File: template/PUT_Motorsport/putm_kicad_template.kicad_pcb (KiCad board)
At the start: 2 copper layers, 60 x 40 mm, 4 parts

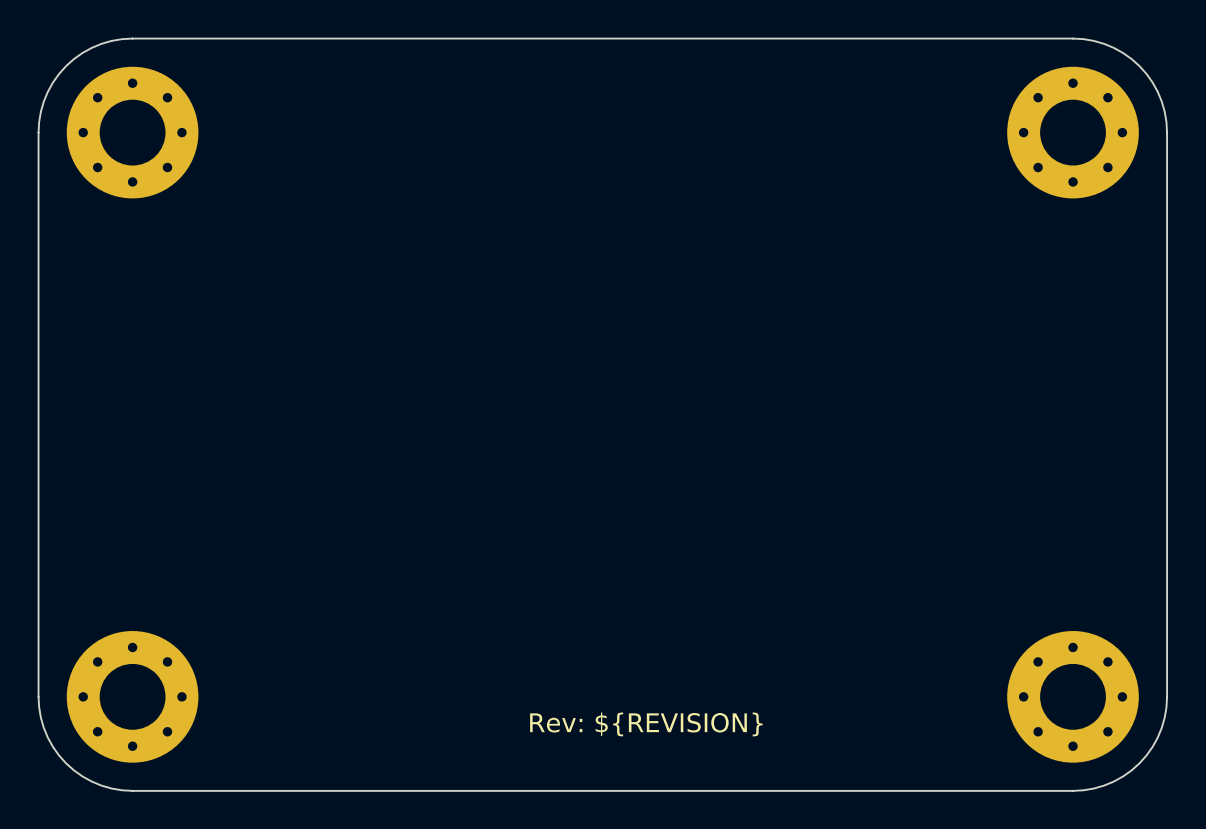
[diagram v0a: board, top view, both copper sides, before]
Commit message: Change mounting holes to M3
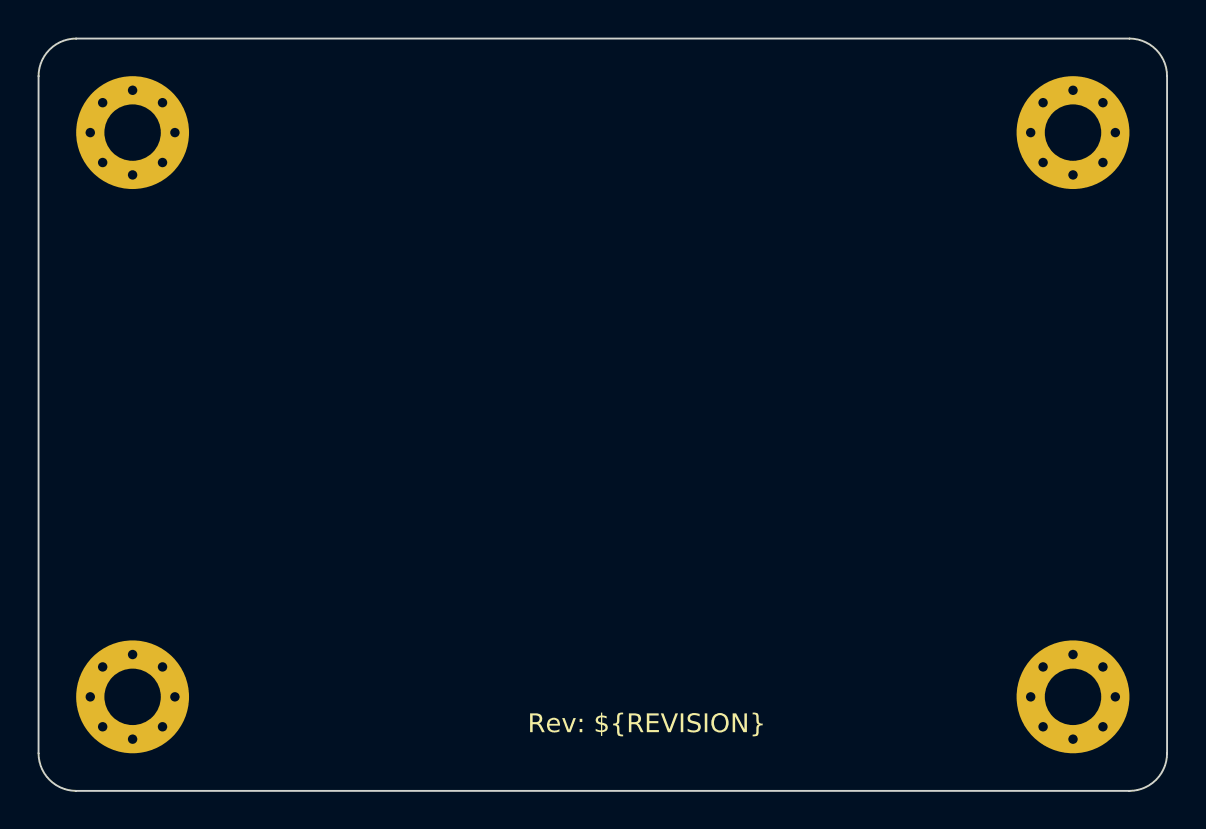
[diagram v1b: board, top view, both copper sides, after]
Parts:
- removed the REF** at (121.0, 81.0)
- removed the REF** at (171.0, 81.0)
- removed the REF** at (171.0, 111.0)
- removed the REF** at (121.0, 111.0)
- added REF**: MountingHole_3mm_Pad_Via, MountingHole:MountingHole_3mm_Pad_Via, F.Cu at (171.0, 81.0)
- added REF**: MountingHole_3mm_Pad_Via, MountingHole:MountingHole_3mm_Pad_Via, F.Cu at (121.0, 111.0)
- added REF**: MountingHole_3mm_Pad_Via, MountingHole:MountingHole_3mm_Pad_Via, F.Cu at (121.0, 81.0)
- added REF**: MountingHole_3mm_Pad_Via, MountingHole:MountingHole_3mm_Pad_Via, F.Cu at (171.0, 111.0)
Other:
- outline, holes or cut-outs redrawn
